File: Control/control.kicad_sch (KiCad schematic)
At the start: 37 parts, among them J1 Conn_01x01, J2 Conn_01x01, J2-J1 Conn_01x10, J3-J1 Conn_01x10, U1 TLV9152IDR, U2 TLV9152IDR, U3 ACS71240KEXBLT-010B3, U4 LP-MSPM0G3507

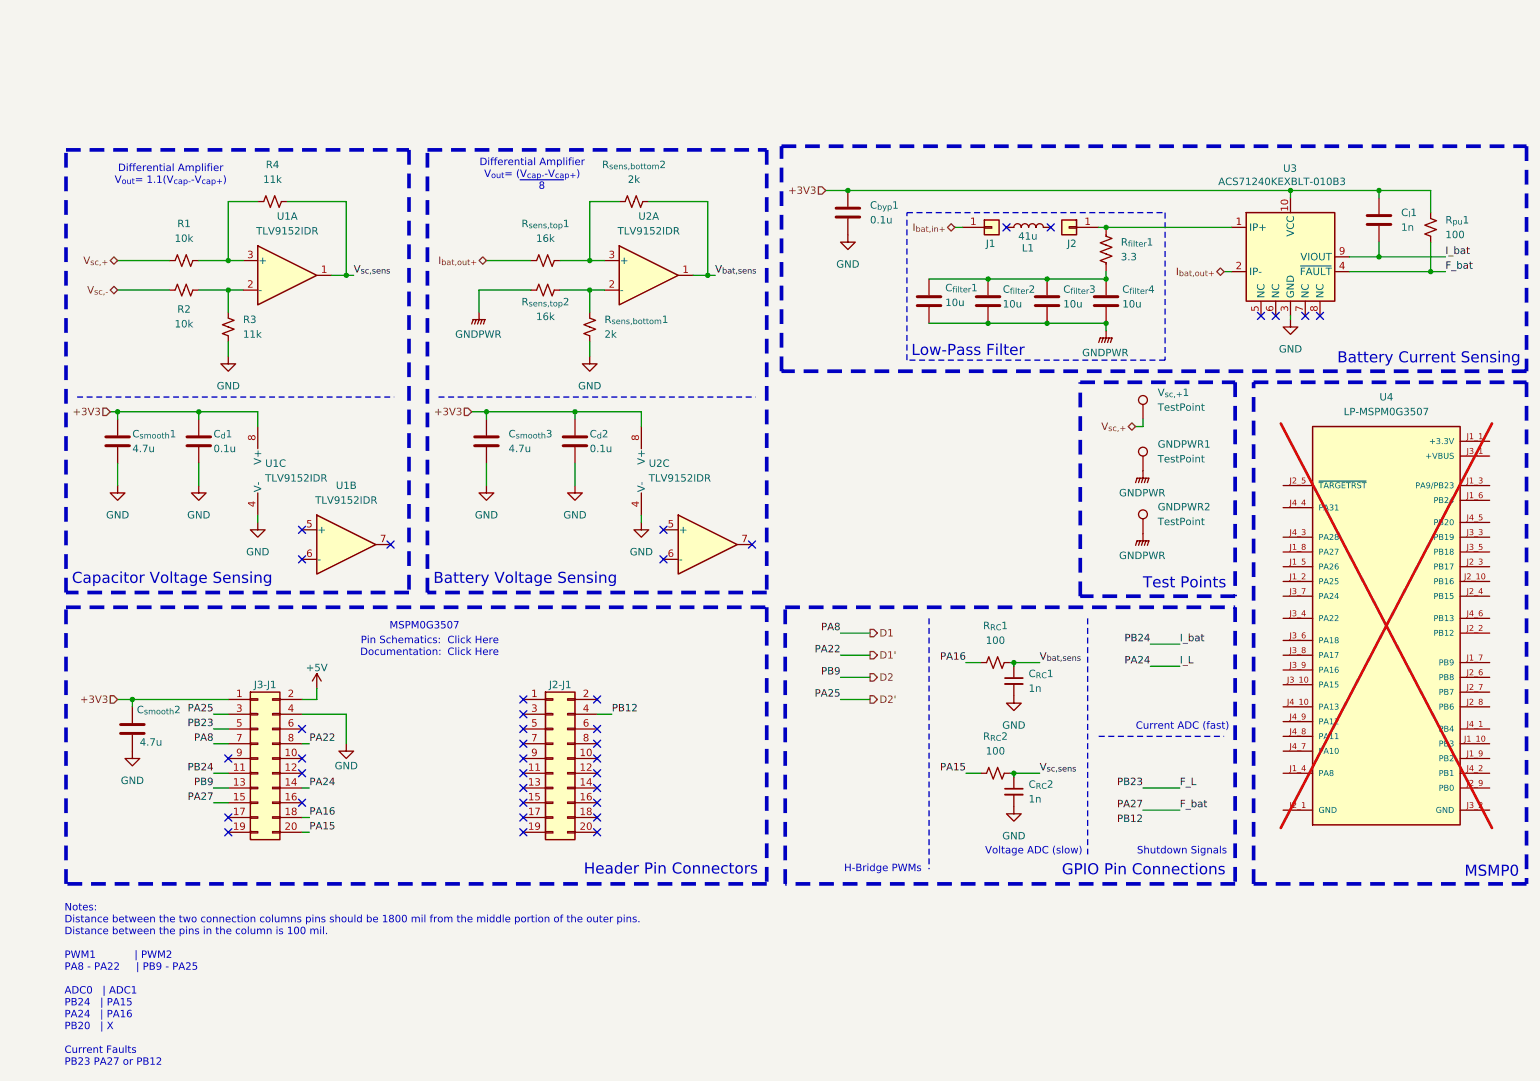
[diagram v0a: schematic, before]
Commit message: added VSSOP 32 chip, todo: change and rewire pinout stuff. see: firmware ccs monkeys
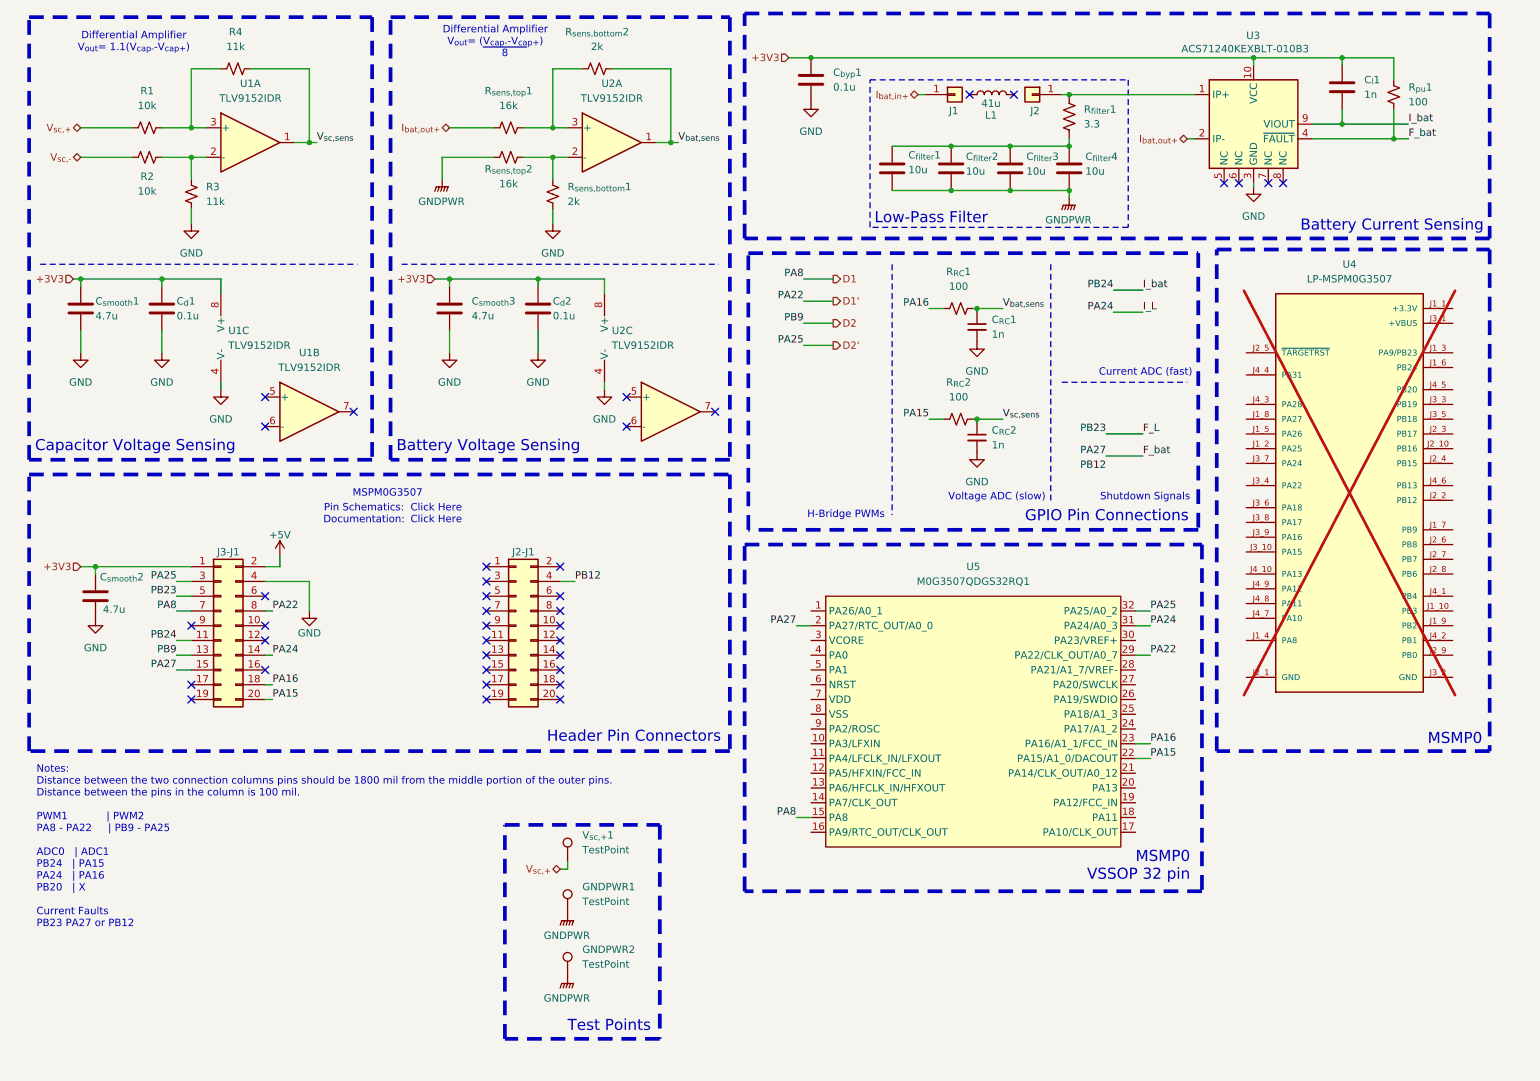
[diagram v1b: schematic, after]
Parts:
- added U5: M0G3507QDGS32RQ1, Robomaster_ICs:VSSOP_0.5mm_32pin_handsolder, symbol Robomaster_Lib:M0G3507QDGS32RQ1
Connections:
- net D1: now also U5.15 (PA8)
- net D1': now also U5.29 (PA22/CLK_OUT/A0_7)
- net D2': now also U5.32 (PA25/A0_2)
- net F_bat: now also U5.2 (PA27/RTC_OUT/A0_0)
- net I_L: now also U5.31 (PA24/A0_3)
- net PA15: now also U5.22 (PA15/A1_0/DACOUT)
- net PA16: now also U5.23 (PA16/A1_1/FCC_IN)
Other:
- note added: "MSMP0 VSSOP 32 pin"
- moved on the sheet: C_{RC}1, C_{RC}2, C_{byp}1, C_{d}1, C_{d}2, C_{filter}1, C_{filter}2, C_{filter}3, C_{filter}4, C_{l}1, C_{smooth}1, C_{smooth}2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
